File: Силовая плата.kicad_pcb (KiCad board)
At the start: 6 copper layers, 66 x 71.8 mm, 69 parts, among them J1 A, J2 B, J3 C, J4 IN-, J5 IN+, J6 Conn_01x10, J7 Conn_01x10, J8 Conn_01x02, J9 A, Q1 2N7002, Q2 2N7002, Q3 2N7002, Q4 2N7002, Q5 2N7002, Q6 2N7002, Q7 BSS214NW

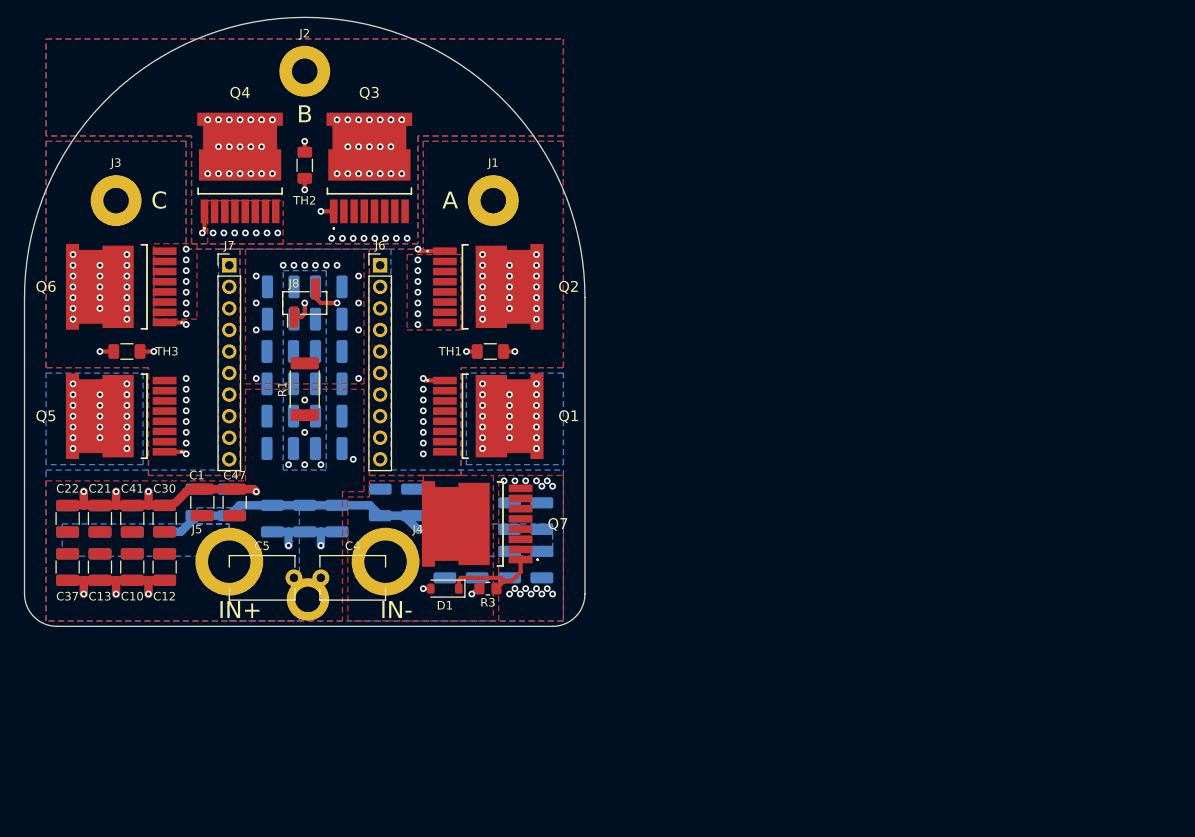
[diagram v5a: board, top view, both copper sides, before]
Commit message: Изменил контур под новую крышку
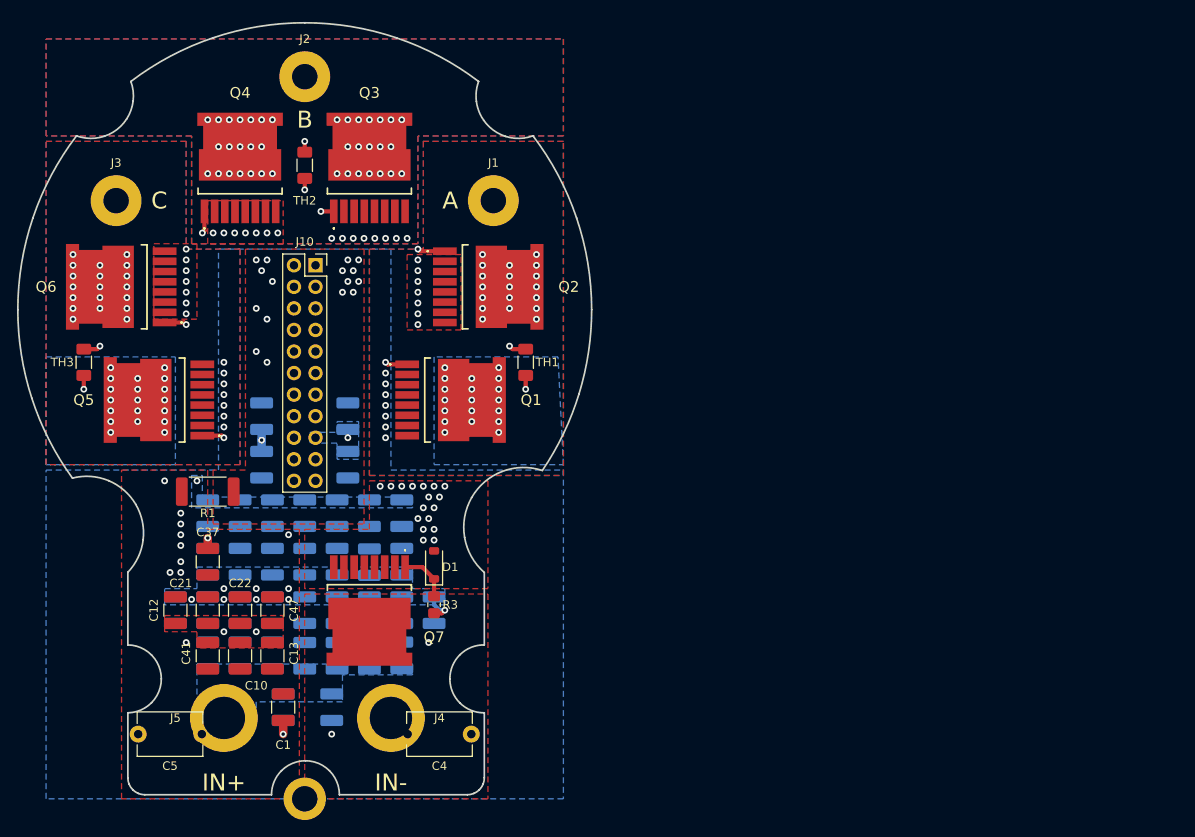
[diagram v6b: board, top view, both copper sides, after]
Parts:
- removed J6, J7: Conn_01x10, Connector_PinHeader_2.54mm:PinHeader_1x10_P2.54mm_Vertical
- removed J8: Conn_01x02, Connector_PinHeader_2.54mm:PinHeader_1x02_P2.54mm_Vertical_SMD_Pin1Left
- added J10: Conn_02x11_Odd_Even, Connector_PinSocket_2.54mm:PinSocket_2x11_P2.54mm_Vertical, F.Cu at (84.5, 90.8)
- C30: moved to B.Cu
- moved C14 49.8 mm to (80.6, 142.9), turned to -90 degrees
- moved C32 35.9 mm to (90.8, 131.4)
- moved C31 35.9 mm to (94.6, 131.4)
- moved C43 32.3 mm to (79.4, 120.0)
- moved C3 32.2 mm to (83.2, 136.8), turned to 90 degrees
- moved C35 31.8 mm to (75.6, 120.0), turned to -90 degrees
- moved C36 31.8 mm to (71.8, 120.0), turned to -90 degrees
- moved J4 30.6 mm to (93.3, 144.1)
- moved J5 30.6 mm to (73.7, 144.1)
- moved C15 30.1 mm to (94.6, 136.8)
- moved C20 29.9 mm to (87.0, 131.4), turned to -90 degrees
- moved C38 29.9 mm to (83.2, 131.4), turned to -90 degrees
- moved C30 29.7 mm to (86.4, 142.9), turned to -90 degrees
- moved C2 28.6 mm to (94.6, 125.7), turned to 90 degrees
- moved C28 28.2 mm to (87.0, 136.8), turned to 90 degrees
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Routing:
- net Shunt_1: track 46.5 -> 14.6 mm, vias 8 -> 17
- net GND: track 152.0 -> 129.6 mm
- net Temp_C: track 12.6 -> 27.3 mm
- net Temp_A: track 11.4 -> 25.7 mm
- net Shunt_2: track 8.04 -> 0.00 mm, vias 71 -> 73
- net G3: track 15.6 -> 8.13 mm
- net G6: track 11.2 -> 17.7 mm
- net G2: track 12.1 -> 18.2 mm
- net Net-(D1-K): track 11.7 -> 6.05 mm
- net G5: track 7.99 -> 13.1 mm
- net Temp_B: track 15.8 -> 10.8 mm
- net A: track 6.40 -> 11.1 mm
- net C: track 5.34 -> 9.31 mm
- net G1: track 8.52 -> 12.5 mm
- net G4: track 15.4 -> 18.5 mm
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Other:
- board size 66 x 71.8 mm -> 67.6 x 91 mm

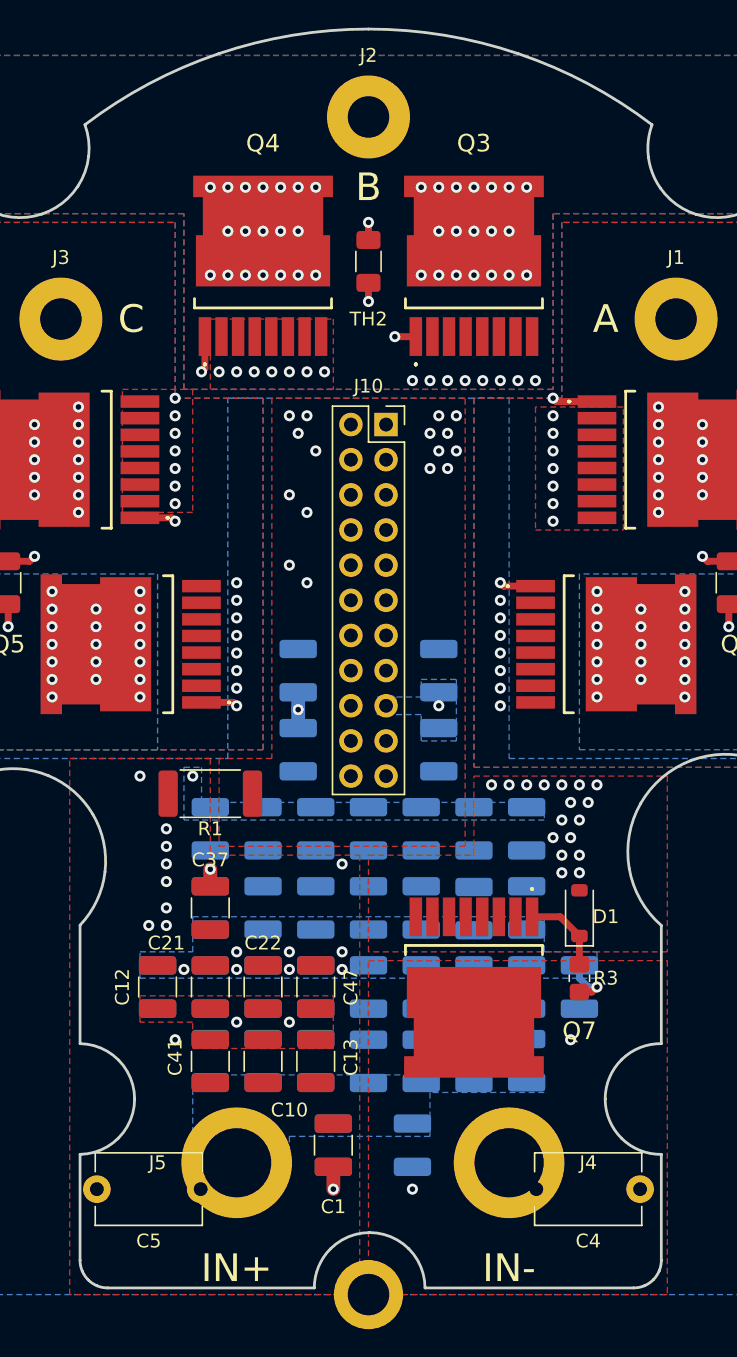
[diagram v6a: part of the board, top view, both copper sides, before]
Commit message: Добавил крепежные отверстия
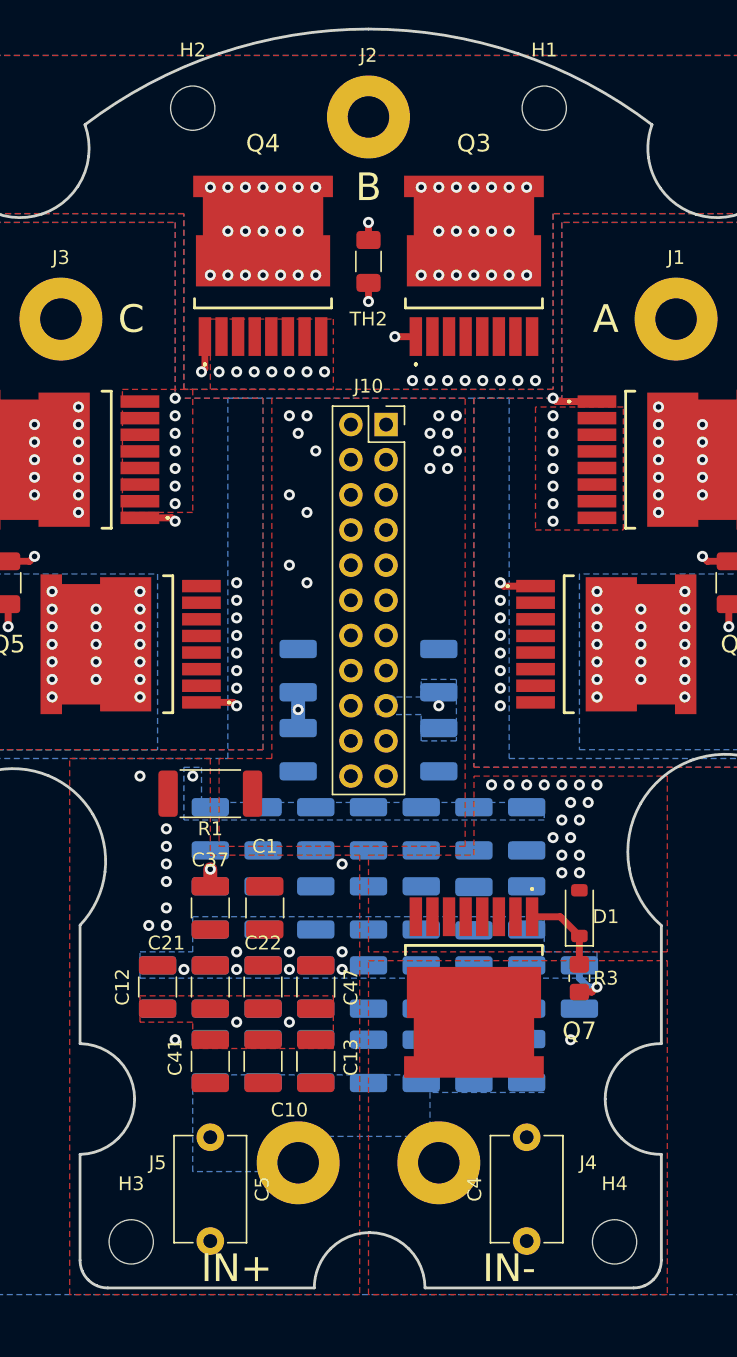
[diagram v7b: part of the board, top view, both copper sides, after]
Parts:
- removed C14, C30: 10u, Capacitor_SMD:C_1210_3225Metric_Pad1.33x2.70mm_HandSolder
- removed J9: A, Connector_My:Power_Wire
- added H1: MountingHole, MountingHole:MountingHole_3.2mm_M3, F.Cu at (95.9, 67.9)
- added H2: MountingHole, MountingHole:MountingHole_3.2mm_M3, F.Cu at (70.5, 67.9)
- added H3: MountingHole, MountingHole:MountingHole_3.2mm_M3, F.Cu at (66.0, 149.9)
- added H4: MountingHole, MountingHole:MountingHole_3.2mm_M3, F.Cu at (101.0, 149.9)
- moved C1 17.8 mm to (75.7, 125.7), turned to 90 degrees
- moved C4 9.01 mm to (94.6, 149.8), turned to 90 degrees
- moved C5 3.81 mm to (71.8, 142.3), turned to -90 degrees
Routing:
- net GND: track 129.6 -> 128.0 mm, vias 51 -> 49

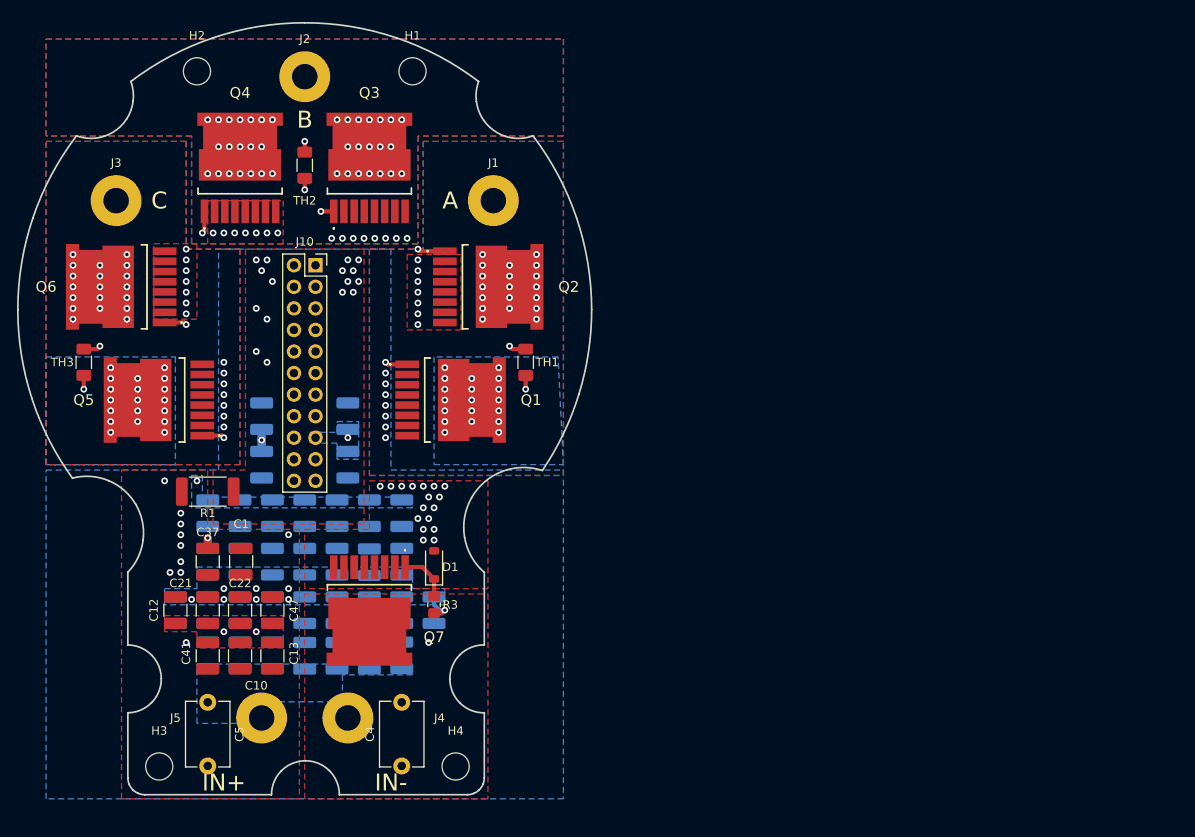
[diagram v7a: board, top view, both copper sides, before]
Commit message: Подрезал края платы под новый контур
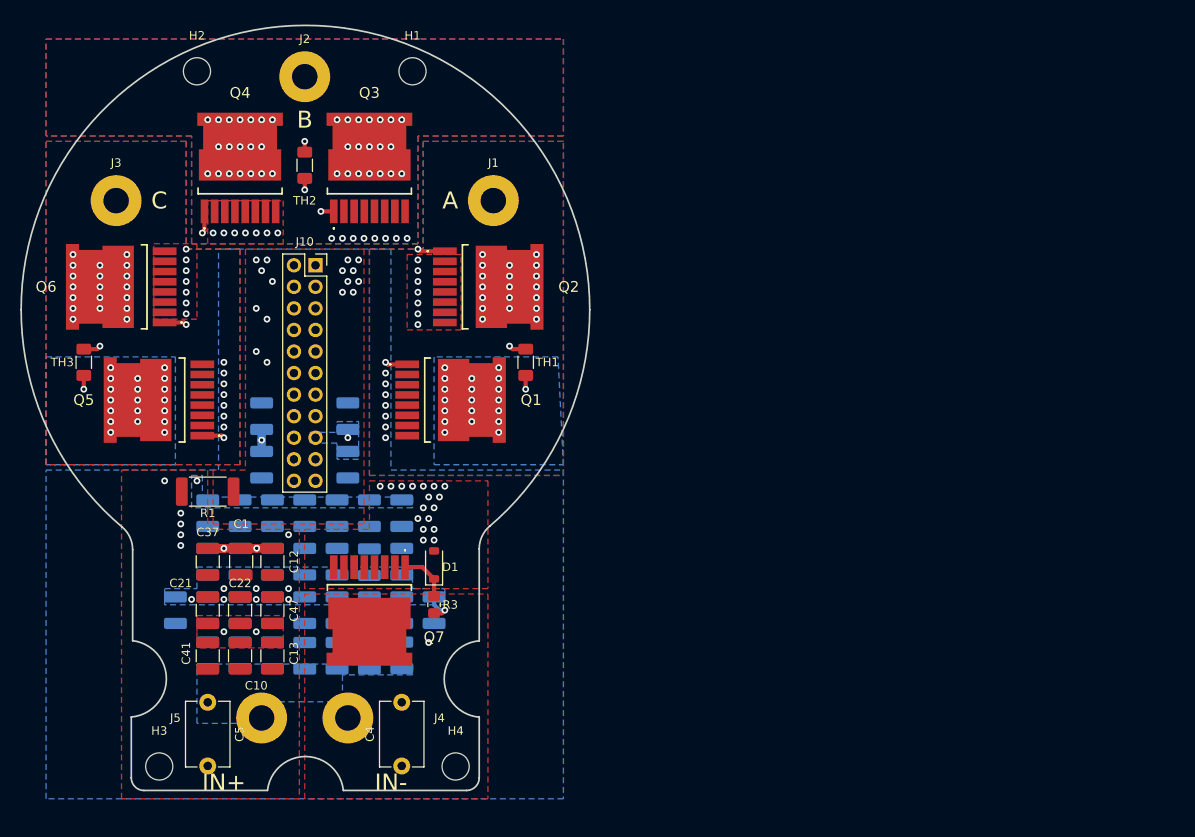
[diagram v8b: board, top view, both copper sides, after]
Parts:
- moved C12 12.8 mm to (79.4, 125.7), turned to 90 degrees
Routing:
- net GND: track 128.0 -> 136.2 mm, vias 49 -> 46
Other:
- board size 67.6 x 91 mm -> 67 x 90.2 mm
